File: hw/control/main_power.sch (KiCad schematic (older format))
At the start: 10 parts, among them U201 LM2596T-ADJ

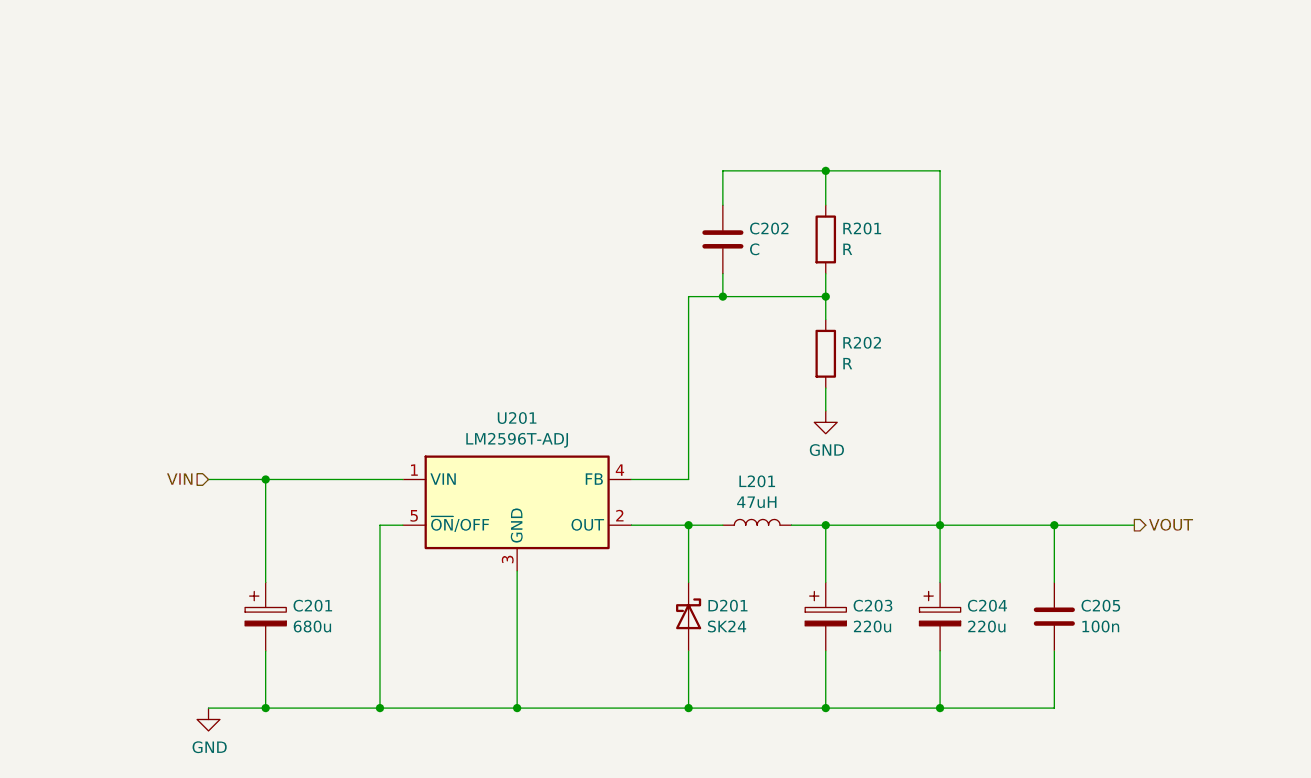
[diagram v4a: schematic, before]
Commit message: [hw] Add some more peripherals
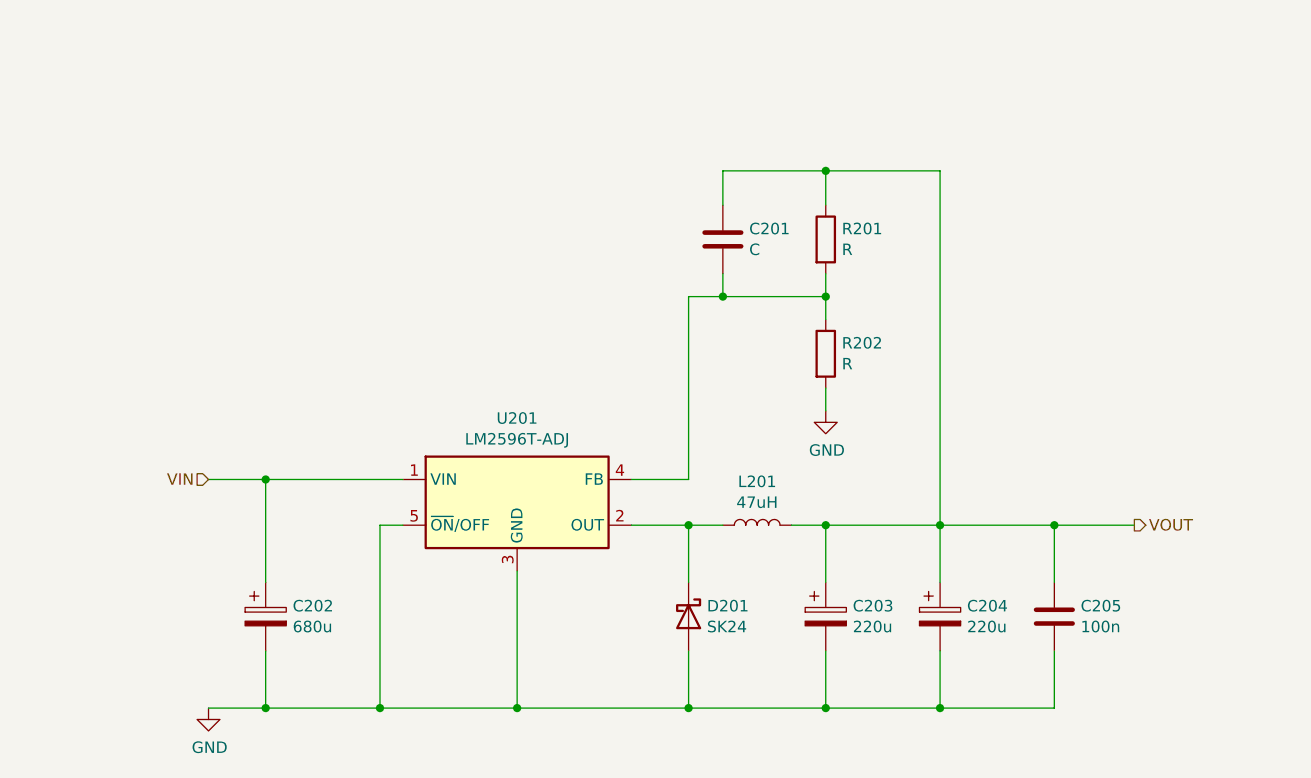
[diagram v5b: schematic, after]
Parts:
- renumbered C202 to C201, C201 to C202
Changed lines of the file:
@@
 $Descr A4 11693 8268
 encoding utf-8
-Sheet 2 9
+Sheet 2 13
 Title "WS2812 Controller"
-Date "2021-09-21"
+Date "2021-10-10"
 Rev "1"
 Comp "Stefan Misik"
@@
 $EndComp
 $Comp
-L Device:CP C201
+L Device:CP C202
 U 1 1 6147E42F
 P 4550 4100
-F 0 "C201" H 4668 4146 50  0000 L CNN
+F 0 "C202" H 4668 4146 50  0000 L CNN
 F 1 "680u" H 4668 4055 50  0000 L CNN
 F 2 "" H 4588 3950 50  0001 C CNN
@@
 	7000 2700 7000 2800
 $Comp
-L Device:C C202
+L Device:C C201
 U 1 1 61484750
 P 6550 2450
-F 0 "C202" H 6665 2496 50  0000 L CNN
+F 0 "C201" H 6665 2496 50  0000 L CNN
 F 1 "C" H 6665 2405 50  0000 L CNN
 F 2 "" H 6588 2300 50  0001 C CNN
@@
 Connection ~ 4550 3500
 $Comp
-L power:GND #PWR0201
+L power:GND #PWR0202
 U 1 1 614AABF3
 P 4300 4500
-F 0 "#PWR0201" H 4300 4250 50  0001 C CNN
+F 0 "#PWR0202" H 4300 4250 50  0001 C CNN
 F 1 "GND" H 4305 4327 50  0000 C CNN
 F 2 "" H 4300 4500 50  0001 C CNN
@@
 Connection ~ 7000 2150
 $Comp
-L power:GND #PWR0202
+L power:GND #PWR0201
 U 1 1 61493959
 P 7000 3200
-F 0 "#PWR0202" H 7000 2950 50  0001 C CNN
+F 0 "#PWR0201" H 7000 2950 50  0001 C CNN
 F 1 "GND" H 7005 3027 50  0000 C CNN
 F 2 "" H 7000 3200 50  0001 C CNN

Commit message: [hw] Assign most of the controller footprints
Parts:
- C201, C205: footprint (none) -> Capacitor_SMD:C_0805_2012Metric_Pad1.18x1.45mm_HandSolder
- D201: footprint (none) -> Diode_SMD:D_SMB_Handsoldering
- L201: footprint (none) -> Inductor_THT:L_Toroid_Vertical_L16.0mm_W8.0mm_P7.62mm
- R201, R202: footprint (none) -> Resistor_SMD:R_0805_2012Metric_Pad1.20x1.40mm_HandSolder
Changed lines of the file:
@@
 F 0 "D201" V 6354 4180 50  0000 L CNN
 F 1 "SK24" V 6445 4180 50  0000 L CNN
-F 2 "" H 6400 4100 50  0001 C CNN
+F 2 "Diode_SMD:D_SMB_Handsoldering" H 6400 4100 50  0001 C CNN
 F 3 "~" H 6400 4100 50  0001 C CNN
 	1    6400 4100
@@
 F 0 "L201" V 6890 3700 50  0000 C CNN
 F 1 "47uH" V 6799 3700 50  0000 C CNN
-F 2 "" H 6700 3700 50  0001 C CNN
+F 2 "Inductor_THT:L_Toroid_Vertical_L16.0mm_W8.0mm_P7.62mm" H 6700 3700 50  0001 C CNN
 F 3 "~" H 6700 3700 50  0001 C CNN
 	1    6700 3700
@@
 F 0 "C205" H 8115 4146 50  0000 L CNN
 F 1 "100n" H 8115 4055 50  0000 L CNN
-F 2 "" H 8038 3950 50  0001 C CNN
+F 2 "Capacitor_SMD:C_0805_2012Metric_Pad1.18x1.45mm_HandSolder" H 8038 3950 50  0001 C CNN
 F 3 "~" H 8000 4100 50  0001 C CNN
 	1    8000 4100
@@
 F 0 "R202" H 7070 2996 50  0000 L CNN
 F 1 "R" H 7070 2905 50  0000 L CNN
-F 2 "" V 6930 2950 50  0001 C CNN
+F 2 "Resistor_SMD:R_0805_2012Metric_Pad1.20x1.40mm_HandSolder" V 6930 2950 50  0001 C CNN
 F 3 "~" H 7000 2950 50  0001 C CNN
 	1    7000 2950
@@
 F 0 "R201" H 7070 2496 50  0000 L CNN
 F 1 "R" H 7070 2405 50  0000 L CNN
-F 2 "" V 6930 2450 50  0001 C CNN
+F 2 "Resistor_SMD:R_0805_2012Metric_Pad1.20x1.40mm_HandSolder" V 6930 2450 50  0001 C CNN
 F 3 "~" H 7000 2450 50  0001 C CNN
 	1    7000 2450
@@
 F 0 "C201" H 6665 2496 50  0000 L CNN
 F 1 "C" H 6665 2405 50  0000 L CNN
-F 2 "" H 6588 2300 50  0001 C CNN
+F 2 "Capacitor_SMD:C_0805_2012Metric_Pad1.18x1.45mm_HandSolder" H 6588 2300 50  0001 C CNN
 F 3 "~" H 6550 2450 50  0001 C CNN
 	1    6550 2450

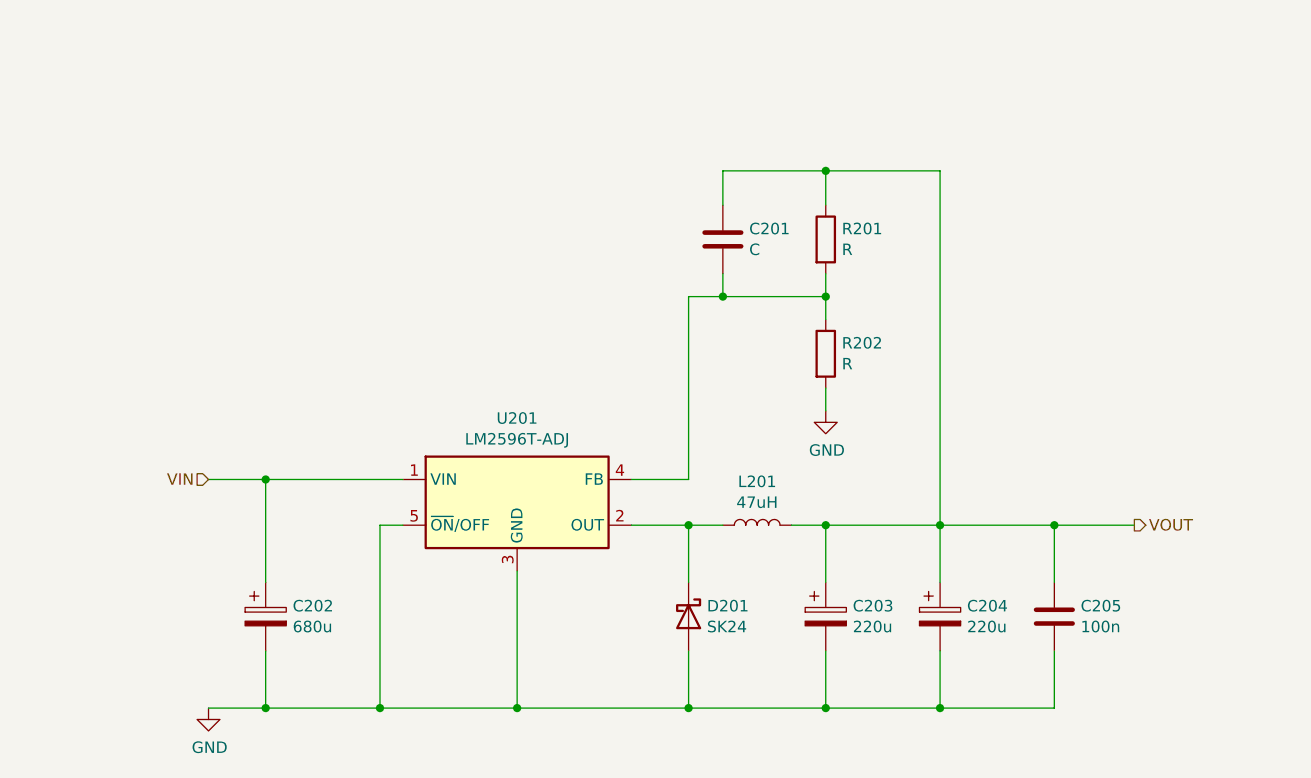
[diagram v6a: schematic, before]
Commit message: [hw] Assign control board footprints
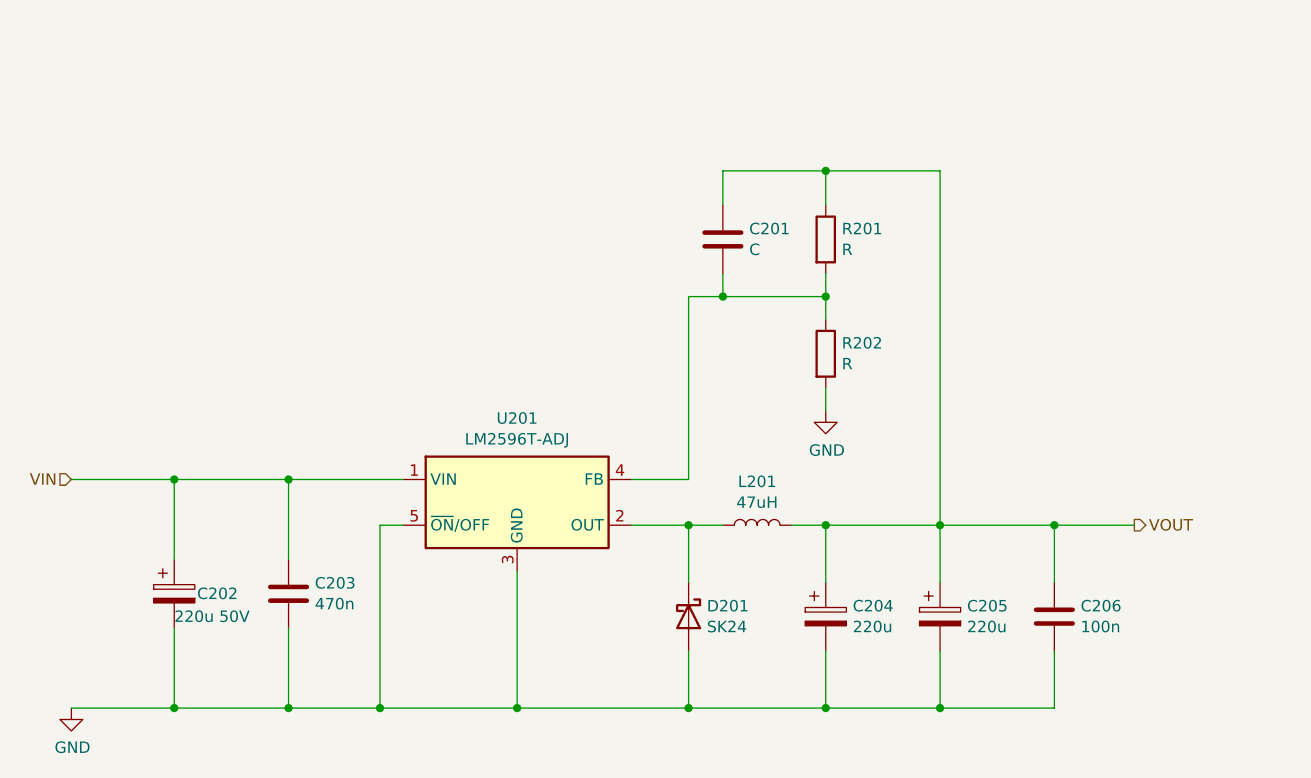
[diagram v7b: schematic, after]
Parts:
- added C203: 470n, Capacitor_SMD:C_0805_2012Metric_Pad1.18x1.45mm_HandSolder, symbol Device:C
- C202: value 680u -> 220u 50V; footprint (none) -> Capacitor_THT:CP_Radial_D10.0mm_P5.00mm
- C204: renamed from C203; footprint (none) -> Capacitor_THT:CP_Radial_D8.0mm_P3.50mm
- C205: renamed from C204; footprint (none) -> Capacitor_THT:CP_Radial_D8.0mm_P3.50mm
- renumbered C205 to C206
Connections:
- net GND: now also C203.2
- net VIN: now also C203.1
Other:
- moved on the sheet: C202
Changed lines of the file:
@@
 Comment4 ""
 $EndDescr
-Text HLabel 4300 3500 0    50   Input ~ 0
+Text HLabel 3700 3500 0    50   Input ~ 0
 VIN
 Text HLabel 8350 3700 2    50   Output ~ 0
@@
 Connection ~ 6400 3700
 $Comp
-L Device:CP C204
+L Device:CP C205
 U 1 1 6147DC54
 P 7500 4100
-F 0 "C204" H 7618 4146 50  0000 L CNN
+F 0 "C205" H 7618 4146 50  0000 L CNN
 F 1 "220u" H 7618 4055 50  0000 L CNN
-F 2 "" H 7538 3950 50  0001 C CNN
+F 2 "Capacitor_THT:CP_Radial_D8.0mm_P3.50mm" H 7538 3950 50  0001 C CNN
 F 3 "~" H 7500 4100 50  0001 C CNN
 	1    7500 4100
@@
 L Device:CP C202
 U 1 1 6147E42F
-P 4550 4100
-F 0 "C202" H 4668 4146 50  0000 L CNN
-F 1 "680u" H 4668 4055 50  0000 L CNN
-F 2 "" H 4588 3950 50  0001 C CNN
-F 3 "~" H 4550 4100 50  0001 C CNN
-	1    4550 4100
-	1    0    0    -1
-$EndComp
-Wire Wire Line
-	4300 4500 4550 4500
-Wire Wire Line
-	4550 4250 4550 4500
-Connection ~ 4550 4500
-Wire Wire Line
-	4550 4500 5050 4500
-Wire Wire Line
-	4550 3950 4550 3500
-Wire Wire Line
-	4550 3500 5150 3500
-$Comp
-L Device:C C205
+P 4150 4000
+F 0 "C202" H 4250 4000 50  0000 L CNN
+F 1 "220u 50V" H 4150 3900 50  0000 L CNN
+F 2 "Capacitor_THT:CP_Radial_D10.0mm_P5.00mm" H 4188 3850 50  0001 C CNN
+F 3 "~" H 4150 4000 50  0001 C CNN
+	1    4150 4000
+	1    0    0    -1
+$EndComp
+Wire Wire Line
+	3700 4500 4150 4500
+Wire Wire Line
+	4150 4150 4150 4500
+Connection ~ 4150 4500
+Wire Wire Line
+	4150 4500 4650 4500
+Wire Wire Line
+	4150 3850 4150 3500
+Wire Wire Line
+	4150 3500 4650 3500
+$Comp
+L Device:C C206
 U 1 1 61480AF3
 P 8000 4100
-F 0 "C205" H 8115 4146 50  0000 L CNN
+F 0 "C206" H 8115 4146 50  0000 L CNN
 F 1 "100n" H 8115 4055 50  0000 L CNN
 F 2 "Capacitor_SMD:C_0805_2012Metric_Pad1.18x1.45mm_HandSolder" H 8038 3950 50  0001 C CNN
@@
 	6550 2150 7000 2150
 Wire Wire Line
-	4300 3500 4550 3500
-Connection ~ 4550 3500
+	3700 3500 4150 3500
+Connection ~ 4150 3500
 $Comp
 L power:GND #PWR0202
 U 1 1 614AABF3
-P 4300 4500
-F 0 "#PWR0202" H 4300 4250 50  0001 C CNN
-F 1 "GND" H 4305 4327 50  0000 C CNN
-F 2 "" H 4300 4500 50  0001 C CNN
-F 3 "" H 4300 4500 50  0001 C CNN
-	1    4300 4500
-	1    0    0    -1
-$EndComp
-$Comp
-L Device:CP C203
+P 3700 4500
+F 0 "#PWR0202" H 3700 4250 50  0001 C CNN
+F 1 "GND" H 3705 4327 50  0000 C CNN
+F 2 "" H 3700 4500 50  0001 C CNN
+F 3 "" H 3700 4500 50  0001 C CNN
+	1    3700 4500
+	1    0    0    -1
+$EndComp
+$Comp
+L Device:CP C204
 U 1 1 6145F282
 P 7000 4100
-F 0 "C203" H 7118 4146 50  0000 L CNN
+F 0 "C204" H 7118 4146 50  0000 L CNN
 F 1 "220u" H 7118 4055 50  0000 L CNN
-F 2 "" H 7038 3950 50  0001 C CNN
+F 2 "Capacitor_THT:CP_Radial_D8.0mm_P3.50mm" H 7038 3950 50  0001 C CNN
 F 3 "~" H 7000 4100 50  0001 C CNN
 	1    7000 4100
@@
 	1    0    0    -1
 $EndComp
+$Comp
+L Device:C C?
+U 1 1 6166DD78
+P 4650 4000
+AR Path="/614AE8DA/6166DD78" Ref="C?"  Part="1"
+AR Path="/614AB031/6166DD78" Ref="C?"  Part="1"
+AR Path="/6147396B/6166DD78" Ref="C203"  Part="1"
+F 0 "C203" H 4765 4046 50  0000 L CNN
+F 1 "470n" H 4765 3955 50  0000 L CNN
+F 2 "Capacitor_SMD:C_0805_2012Metric_Pad1.18x1.45mm_HandSolder" H 4688 3850 50  0001 C CNN
+F 3 "~" H 4650 4000 50  0001 C CNN
+	1    4650 4000
+	1    0    0    -1
+$EndComp
+Wire Wire Line
+	4650 3850 4650 3500
+Wire Wire Line
+	4650 4150 4650 4500
+Connection ~ 4650 4500
+Wire Wire Line
+	4650 4500 5050 4500
+Connection ~ 4650 3500
+Wire Wire Line
+	4650 3500 5150 3500
 $EndSCHEMATC

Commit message: [hw] Incorporate suggestions
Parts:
- added D?: D_Schottky, symbol Device:D_Schottky
- added D?: 1.5KExxA, Diode_THT:D_DO-201AE_P15.24mm_Horizontal, symbol Diode:1.5KExxA
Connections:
- net GND: now also D?.2 (A2)
- net VIN: now also D?.1 (K)
- net VOUT: now also D?.1 (A1), D?.2 (A)
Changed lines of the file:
@@
 Text HLabel 3700 3500 0    50   Input ~ 0
 VIN
-Text HLabel 8350 3700 2    50   Output ~ 0
+Text HLabel 8750 3700 2    50   Output ~ 0
 VOUT
 $Comp
@@
 	8000 3700 8000 3950
 Connection ~ 7500 3700
-Wire Wire Line
-	8000 3700 8350 3700
 Connection ~ 8000 3700
 Wire Wire Line
@@
 Wire Wire Line
 	4650 3500 5150 3500
+$Comp
+L Device:D_Schottky D?
+U 1 1 616D9BA9
+P 5650 1750
+F 0 "D?" H 5650 1967 50  0000 C CNN
+F 1 "D_Schottky" H 5650 1876 50  0000 C CNN
+F 2 "" H 5650 1750 50  0001 C CNN
+F 3 "~" H 5650 1750 50  0001 C CNN
+	1    5650 1750
+	1    0    0    -1
+$EndComp
+Wire Wire Line
+	5800 1750 8000 1750
+Wire Wire Line
+	8000 1750 8000 3700
+Wire Wire Line
+	8000 3700 8450 3700
+Wire Wire Line
+	5500 1750 4150 1750
+Wire Wire Line
+	4150 1750 4150 3500
+$Comp
+L Diode:1.5KExxA D?
+U 1 1 616DE797
+P 8450 4100
+F 0 "D?" V 8404 4180 50  0000 L CNN
+F 1 "1.5KExxA" V 8495 4180 50  0000 L CNN
+F 2 "Diode_THT:D_DO-201AE_P15.24mm_Horizontal" H 8450 3900 50  0001 C CNN
+F 3 "https://www.vishay.com/docs/88301/15ke.pdf" H 8400 4100 50  0001 C CNN
+	1    8450 4100
+	0    1    1    0
+$EndComp
+Wire Wire Line
+	8450 3950 8450 3700
+Connection ~ 8450 3700
+Wire Wire Line
+	8450 3700 8750 3700
+Wire Wire Line
+	8450 4250 8450 4500
+Wire Wire Line
+	8450 4500 8000 4500
+Connection ~ 8000 4500
 $EndSCHEMATC
